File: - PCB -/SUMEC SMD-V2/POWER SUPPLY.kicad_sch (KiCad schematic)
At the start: 7 parts, among them U7 LM1084IS-5.0/NOPB, U8 LM1084IS-3.3/NOPB

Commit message: cleanup
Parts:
- IC?: footprint sumec_library:AMASS_XT30U-M_1x02_P5.0mm_Vertical -> (none)
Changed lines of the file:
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@@
       (effects (font (size 1.27 1.27)))
     )
-    (property "Footprint" "sumec_library:AMASS_XT30U-M_1x02_P5.0mm_Vertical" (at 157.48 121.92 0)
+    (property "Footprint" "" (at 157.48 121.92 0)
       (effects (font (size 1.27 1.27)) (justify left) hide)
     )

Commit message: sumec SMD V2 schematic update
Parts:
- removed U8: LM1084IS-3.3/NOPB, Package_TO_SOT_SMD:TO-263-3_TabPin4, symbol Regulator_Linear:LM1084-3.3
- added U6: LM1084IS-5.0/NOPB, Package_TO_SOT_SMD:TO-263-3_TabPin4, symbol Regulator_Linear:LM1084-3.3
- C10, C11, C12, C13: footprint (none) -> Capacitor_SMD:CP_Elec_4x5.8
- IC?: footprint (none) -> sumec-smdV2_library:XT30U-M_1x02_P5.0mm_Vertical
- U7: value LM1084IS-5.0/NOPB -> LM1084IS-3.3/NOPB
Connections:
- net +3V3: now also U7.2 (VO)
- net +5V: now also U7.3 (VI), U6.2 (VO); no longer U7.2 (VO)
- net +8V: now also U6.3 (VI); no longer U7.3 (VI)
- net GND: now also U6.1 (GND)
- no-connect marks 0 -> 1
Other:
- note added: "5A, 3.3V"
- note added: "5A, 5V"
- note added: "STABILISER"
- note added: "TO-263-3"
- note added: "XT30M CONNECTOR"
- note added: "budeme mit 12V friendly board - novy motory"
- note added: "nejvetsi soucastka na boardu"
- note added: "pouzivat tantal/elektrolyt"
- note added: "pridat text"
- note removed: "STABILIZATOR"
- note removed: "XT30M KONEKTOR"

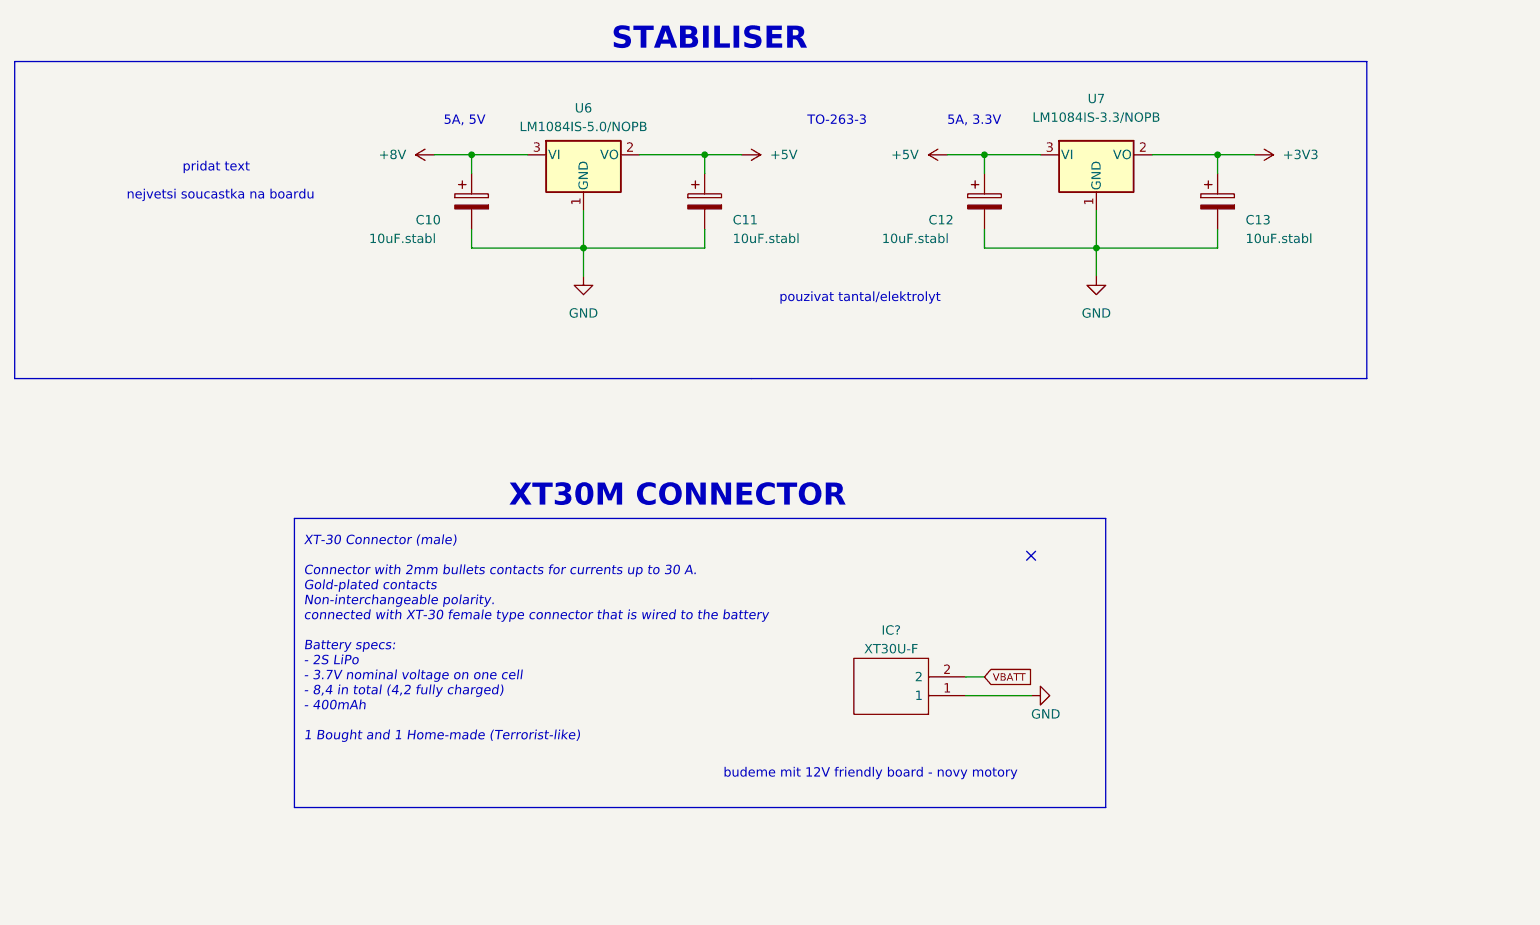
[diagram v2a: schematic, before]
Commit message: Updates:
GyroScope project file, QRE1113 Board update and BOM, SMDv2 iBOM and schematic update.
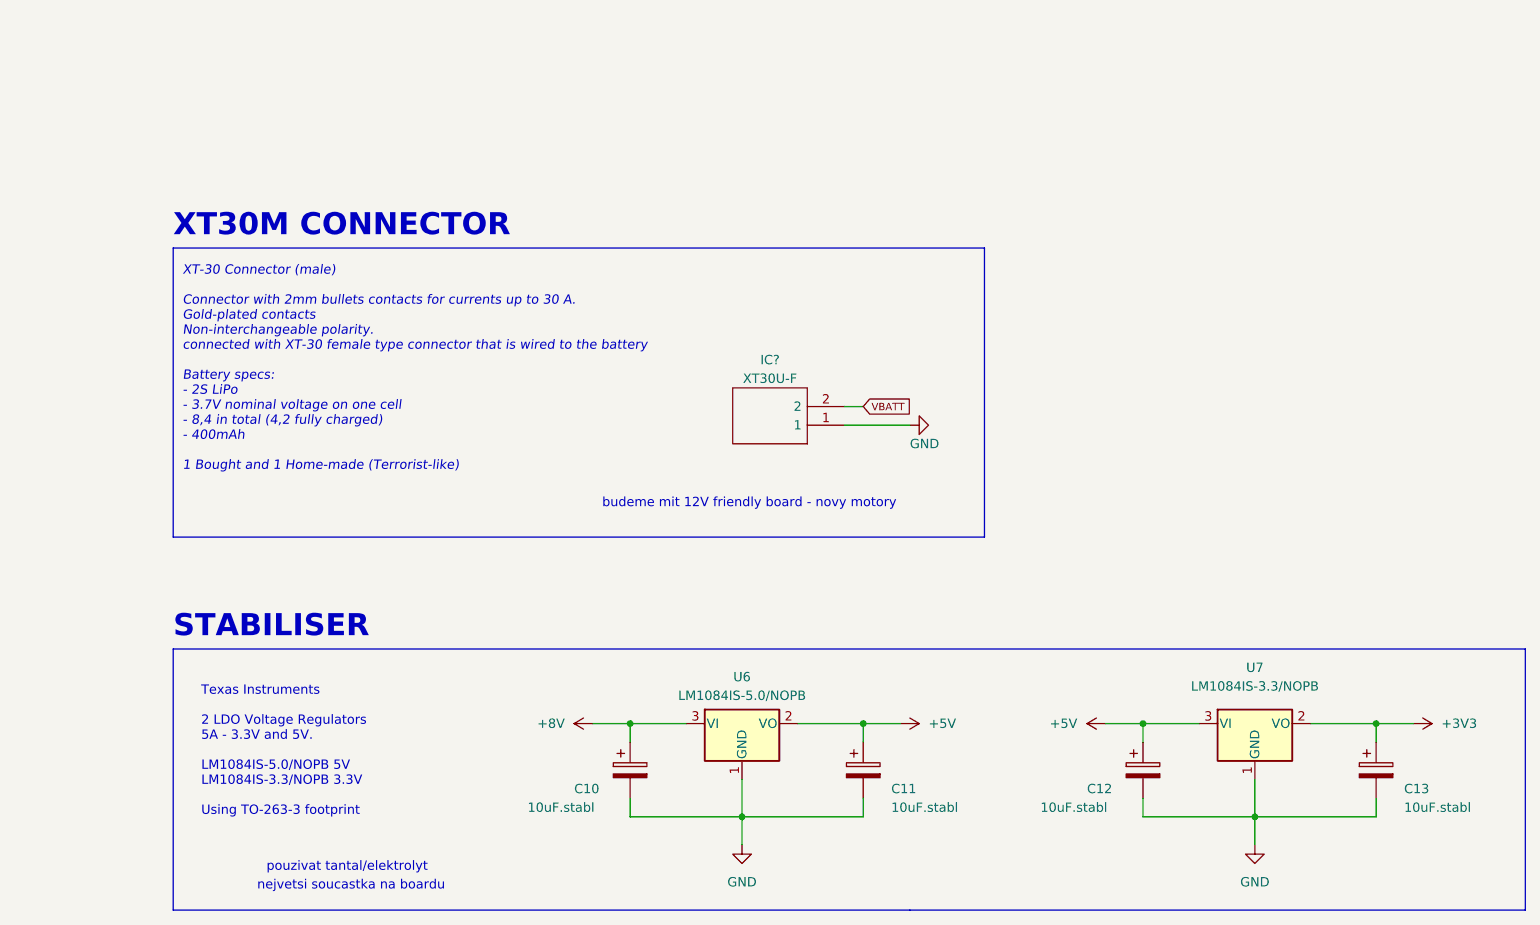
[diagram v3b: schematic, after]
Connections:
- no-connect marks 1 -> 0
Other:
- note added: "Texas Instruments 2 LDO Voltage Regulators 5A - 3.3V and 5V. LM1084IS-5.0/NOPB 5V LM1084IS-3.3/NOPB 3.3V Using TO-263-3 footprint"
- note removed: "5A, 3.3V"
- note removed: "5A, 5V"
- note removed: "TO-263-3"
- note removed: "pridat text"
- moved on the sheet: C10, C11, C12, C13, IC?, U6, U7

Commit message: schematic miniupdate
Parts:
- removed U6: LM1084IS-5.0/NOPB, Package_TO_SOT_SMD:TO-263-3_TabPin4, symbol Regulator_Linear:LM1084-3.3
- removed U7: LM1084IS-3.3/NOPB, Package_TO_SOT_SMD:TO-263-3_TabPin4, symbol Regulator_Linear:LM1084-3.3
- added U1: LM1084-3.3, Package_TO_SOT_SMD:TO-263-3_TabPin2, symbol Regulator_Linear:LM1084-3.3
- added U4: LM1084-5.0, Package_TO_SOT_SMD:TO-263-3_TabPin2, symbol Regulator_Linear:LM1084-5.0
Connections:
- net +3V3: now also U1.2 (VO)
- net +5V: now also U1.3 (VI), U4.2 (VO)
- net GND: now also U1.1 (GND), U4.1 (GND)
- net +8V renamed +12V
- net +12V: now also U4.3 (VI)

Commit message: New switch
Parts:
- C10, C11, C12, C13: footprint Capacitor_SMD:CP_Elec_4x5.8 -> Capacitor_SMD:C_0805_2012Metric_Pad1.18x1.45mm_HandSolder
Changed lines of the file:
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@@
       (effects (font (size 1.27 1.27)) (justify left))
     )
-    (property "Footprint" "Capacitor_SMD:CP_Elec_4x5.8" (at 129.2352 133.35 0)
+    (property "Footprint" "Capacitor_SMD:C_0805_2012Metric_Pad1.18x1.45mm_HandSolder" (at 129.2352 133.35 0)
       (effects (font (size 1.27 1.27)) hide)
     )
@@
       (effects (font (size 1.27 1.27)) (justify left))
     )
-    (property "Footprint" "Capacitor_SMD:CP_Elec_4x5.8" (at 230.8352 133.35 0)
+    (property "Footprint" "Capacitor_SMD:C_0805_2012Metric_Pad1.18x1.45mm_HandSolder" (at 230.8352 133.35 0)
       (effects (font (size 1.27 1.27)) hide)
     )
@@
       (effects (font (size 1.27 1.27)) (justify left))
     )
-    (property "Footprint" "Capacitor_SMD:CP_Elec_4x5.8" (at 160.9852 133.35 0)
+    (property "Footprint" "Capacitor_SMD:C_0805_2012Metric_Pad1.18x1.45mm_HandSolder" (at 160.9852 133.35 0)
       (effects (font (size 1.27 1.27)) hide)
     )
@@
       (effects (font (size 1.27 1.27)) (justify left))
     )
-    (property "Footprint" "Capacitor_SMD:CP_Elec_4x5.8" (at 199.0852 133.35 0)
-      (effects (font (size 1.27 1.27)) hide)
-    )
+    (property "Footprint" "Capacitor_SMD:C_0805_2012Metric_Pad1.18x1.45mm_HandSolder" (at 199.0852 133.35 0)
+      (effects (font (size 1.27 1.27)) hide)
+    )

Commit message: Borard upd
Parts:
- C10, C11, C12, C13: footprint Capacitor_SMD:C_0805_2012Metric_Pad1.18x1.45mm_HandSolder -> Capacitor_Tantalum_SMD:CP_EIA-2012-12_Kemet-R_Pad1.30x1.05mm_HandSolder
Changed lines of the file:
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@@
       (effects (font (size 1.27 1.27)) (justify left))
     )
-    (property "Footprint" "Capacitor_SMD:C_0805_2012Metric_Pad1.18x1.45mm_HandSolder" (at 129.2352 133.35 0)
+    (property "Footprint" "Capacitor_Tantalum_SMD:CP_EIA-2012-12_Kemet-R_Pad1.30x1.05mm_HandSolder" (at 129.2352 133.35 0)
       (effects (font (size 1.27 1.27)) hide)
     )
@@
       (effects (font (size 1.27 1.27)) (justify left))
     )
-    (property "Footprint" "Capacitor_SMD:C_0805_2012Metric_Pad1.18x1.45mm_HandSolder" (at 230.8352 133.35 0)
+    (property "Footprint" "Capacitor_Tantalum_SMD:CP_EIA-2012-12_Kemet-R_Pad1.30x1.05mm_HandSolder" (at 230.8352 133.35 0)
       (effects (font (size 1.27 1.27)) hide)
     )
@@
       (effects (font (size 1.27 1.27)) (justify left))
     )
-    (property "Footprint" "Capacitor_SMD:C_0805_2012Metric_Pad1.18x1.45mm_HandSolder" (at 160.9852 133.35 0)
+    (property "Footprint" "Capacitor_Tantalum_SMD:CP_EIA-2012-12_Kemet-R_Pad1.30x1.05mm_HandSolder" (at 160.9852 133.35 0)
       (effects (font (size 1.27 1.27)) hide)
     )
@@
       (effects (font (size 1.27 1.27)) (justify left))
     )
-    (property "Footprint" "Capacitor_SMD:C_0805_2012Metric_Pad1.18x1.45mm_HandSolder" (at 199.0852 133.35 0)
-      (effects (font (size 1.27 1.27)) hide)
-    )
+    (property "Footprint" "Capacitor_Tantalum_SMD:CP_EIA-2012-12_Kemet-R_Pad1.30x1.05mm_HandSolder" (at 199.0852 133.35 0)
+      (effects (font (size 1.27 1.27)) hide)
+    )

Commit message: Board Update
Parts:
- removed IC?: XT30U-F, sumec-smdV2_library:XT30U-M_1x02_P5.0mm_Vertical, symbol SamacSys_Parts:XT30U-M
- added J11: XT30PW-M, sumec-smdV2_library:AMASS_XT30PW-M, symbol sumec_library:XT30PW-M
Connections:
- net GND: now also J11.N
- net VBATT: now also J11.P
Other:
- note removed: "budeme mit 12V friendly board - novy motory"
- note removed: "nejvetsi soucastka na boardu"
- note removed: "pouzivat tantal/elektrolyt"
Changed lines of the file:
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@@
     (effects (font (size 1.27 1.27)) (justify left bottom))
-  )
-  (text "budeme mit 12V friendly board - novy motory " (at 124.46 93.98 0)
-    (effects (font (size 1.27 1.27) (color 255 0 0 1)) (justify left bottom))
   )
   (text "XT-30 Connector (male)\n\nConnector with 2mm bullets contacts for currents up to 30 A.\nGold-plated contacts\nNon-interchangeable polarity.\nconnected with XT-30 female type connector that is wired to the battery\n\nBattery specs:\n- 2S LiPo\n- 3.7V nominal voltage on one cell\n- 8,4 in total (4,2 fully charged)\n- 400mAh \n\n1 Bought and 1 Home-made (Terrorist-like)"
     (at 67.31 88.9 0)
     (effects (font (size 1.27 1.27) italic) (justify left bottom))
-  )
-  (text "nejvetsi soucastka na boardu" (at 77.47 146.05 0)
-    (effects (font (size 1.27 1.27) (color 255 0 0 1)) (justify left bottom))
-  )
-  (text "pouzivat tantal/elektrolyt " (at 78.74 143.51 0)
-    (effects (font (size 1.27 1.27) (color 255 0 0 1)) (justify left bottom))
   )
   (text "STABILISER" (at 66.04 111.76 0)
@@
     )
   )
+  (symbol (lib_id "sumec_library:XT30PW-M") (at 152.4 80.01 0) (unit 1)
+    (in_bom yes) (on_board yes) (dnp no) (fields_autoplaced)
+    (property "Reference" "J11" (at 148.59 73.66 0)
+      (effects (font (size 1.27 1.27)))
+    )
+    (property "Value" "XT30PW-M" (at 148.59 76.2 0)
+      (effects (font (size 1.27 1.27)))
+    )
+    (property "Footprint" "sumec-smdV2_library:AMASS_XT30PW-M" (at 152.4 80.01 0)
+      (effects (font (size 1.27 1.27)) (justify bottom) hide)
+    )
+    (property "Datasheet" "" (at 152.4 80.01 0)
+      (effects (font (size 1.27 1.27)) hide)
+    )
+    (property "MF" "AMASS" (at 152.4 80.01 0)
+      (effects (font (size 1.27 1.27)) (justify bottom) hide)
+    )
+    (property "MAXIMUM_PACKAGE_HEIGHT" "5 mm" (at 152.4 80.01 0)
+      (effects (font (size 1.27 1.27)) (justify bottom) hide)
+    )
+    (property "Package" "None" (at 152.4 80.01 0)
+      (effects (font (size 1.27 1.27)) (justify bottom) hide)
+    )
+    (property "Price" "None" (at 152.4 80.01 0)
+      (effects (font (size 1.27 1.27)) (justify bottom) hide)
+    )
+    (property "Check_prices" "https://www.snapeda.com/parts/XT30PW-M/AMASS/view-part/?ref=eda" (at 152.4 80.01 0)
+      (effects (font (size 1.27 1.27)) (justify bottom) hide)
+    )
+    (property "STANDARD" "Manufacturer Recommendations" (at 152.4 80.01 0)
+      (effects (font (size 1.27 1.27)) (justify bottom) hide)
+    )
+    (property "PARTREV" "1.2" (at 152.4 80.01 0)
+      (effects (font (size 1.27 1.27)) (justify bottom) hide)
+    )
+    (property "SnapEDA_Link" "https://www.snapeda.com/parts/XT30PW-M/AMASS/view-part/?ref=snap" (at 152.4 80.01 0)
+      (effects (font (size 1.27 1.27)) (justify bottom) hide)
+    )
+    (property "MP" "XT30PW-M" (at 152.4 80.01 0)
+      (effects (font (size 1.27 1.27)) (justify bottom) hide)
+    )
+    (property "Description" "\nSocket; DC supply; XT30; male; PIN: 2; on PCBs; THT; Colour: yellow\n" (at 152.4 80.01 0)
+      (effects (font (size 1.27 1.27)) (justify bottom) hide)
+    )
+    (property "MANUFACTURER" "Amass" (at 152.4 80.01 0)
+      (effects (font (size 1.27 1.27)) (justify bottom) hide)
+    )
+    (property "Availability" "Not in stock" (at 152.4 80.01 0)
+      (effects (font (size 1.27 1.27)) (justify bottom) hide)
+    )
+    (property "SNAPEDA_PN" "XT30PW-M" (at 152.4 80.01 0)
+      (effects (font (size 1.27 1.27)) (justify bottom) hide)
+    )
+    (pin "N")
+    (pin "P")
+    (instances
+      (project "sumec"
+        (path "/fc70a1a8-ed7c-4a0f-9b1a-f23293528385/2febd48c-c6ec-477b-ac64-6fa98a41fff0"
+          (reference "J11") (unit 1)
+        )
+      )
+    )
+  )
   (symbol (lib_id "Device:C_Polarized") (at 229.87 129.54 0) (unit 1)
     (in_bom yes) (on_board yes) (dnp no)
@@
         )
       )
-    )
-  )
-  (symbol (lib_id "SamacSys_Parts:XT30U-M") (at 157.48 82.55 180) (unit 1)
-    (in_bom yes) (on_board yes) (dnp no) (fields_autoplaced)
-    (property "Reference" "IC?" (at 147.32 73.66 0)
-      (effects (font (size 1.27 1.27)))
-    )
-    (property "Value" "XT30U-F" (at 147.32 76.2 0)
-      (effects (font (size 1.27 1.27)))
-    )
-    (property "Footprint" "sumec-smdV2_library:XT30U-M_1x02_P5.0mm_Vertical" (at 140.97 85.09 0)
-      (effects (font (size 1.27 1.27)) (justify left) hide)
-    )
-    (property "Datasheet" "https://www.tme.eu/Document/3cbfa5cfa544d79584972dd5234a409e/XT30U%20SPEC.pdf" (at 140.97 82.55 0)
-      (effects (font (size 1.27 1.27)) (justify left) hide)
-    )
-    (property "Description" "Plug; DC supply; XT30; male; PIN: 2; for cable; soldering; 15A; 500V" (at 140.97 80.01 0)
-      (effects (font (size 1.27 1.27)) (justify left) hide)
-    )
-    (property "Height" "10.7" (at 140.97 77.47 0)
-      (effects (font (size 1.27 1.27)) (justify left) hide)
-    )
-    (property "Manufacturer_Name" "Amass" (at 140.97 74.93 0)
-      (effects (font (size 1.27 1.27)) (justify left) hide)
-    )
-    (property "Manufacturer_Part_Number" "XT30U-M" (at 140.97 72.39 0)
-      (effects (font (size 1.27 1.27)) (justify left) hide)
-    )
-    (property "Mouser Part Number" "" (at 140.97 69.85 0)
-      (effects (font (size 1.27 1.27)) (justify left) hide)
-    )
-    (property "Mouser Price/Stock" "" (at 140.97 67.31 0)
-      (effects (font (size 1.27 1.27)) (justify left) hide)
-    )
-    (property "Arrow Part Number" "" (at 140.97 64.77 0)
-      (effects (font (size 1.27 1.27)) (justify left) hide)
-    )
-    (property "Arrow Price/Stock" "" (at 140.97 62.23 0)
-      (effects (font (size 1.27 1.27)) (justify left) hide)
-    )
-    (property "Mouser Testing Part Number" "" (at 140.97 59.69 0)
-      (effects (font (size 1.27 1.27)) (justify left) hide)
-    )
-    (property "Mouser Testing Price/Stock" "" (at 140.97 57.15 0)
-      (effects (font (size 1.27 1.27)) (justify left) hide)
-    )
-    (property "LCSC" "C99101" (at 157.48 82.55 0)
-      (effects (font (size 1.27 1.27)) hide)
-    )
-    (pin "1")
-    (pin "2")
-    (instances
-      (project "sumec"
-        (path "/fc70a1a8-ed7c-4a0f-9b1a-f23293528385"
-          (reference "IC?") (unit 1)
-        )
-        (path "/fc70a1a8-ed7c-4a0f-9b1a-f23293528385/2febd48c-c6ec-477b-ac64-6fa98a41fff0"
-          (reference "IC1") (unit 1)
-        )
-      )
